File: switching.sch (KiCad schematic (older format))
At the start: 0 parts

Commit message: Added switching, still need arduino verification, need buffer, consisder PSU polarity switch
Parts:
- added D? (x4): 1N914, symbol Device:D
- added J?: Screw_Terminal_01x05, symbol Connector:Screw_Terminal_01x05
- added K? (x4): RM50-xx21, Relay_THT:Relay_SPST_Finder_32.21-x300, symbol Relay:RM50-xx21
- added Q? (x4): 2N3904, Package_TO_SOT_THT:TO-92_Inline, symbol Transistor_BJT:2N3904
- added R? (x4): 1k, symbol Device:R
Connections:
- new net: J?.1 (Pin_1), K?.11
- new net: J?.5 (Pin_5), K?.14, K?.14, K?.14, K?.14
- new net: D?.2 (A), K?.A1, Q?.3 (C) (x4)
- new net: J?.2 (Pin_2), K?.11
- new net: J?.3 (Pin_3), K?.11
- new net: J?.4 (Pin_4), K?.11
- new net: Q?.2 (B), R?.1 (x4)
- new net +9V: D?.1 (K), D?.1 (K), D?.1 (K), D?.1 (K), K?.A2, K?.A2, K?.A2, K?.A2
- new net GND: Q?.1 (E), Q?.1 (E), Q?.1 (E), Q?.1 (E)
- new net RLY0: R?.2
- new net RLY1: R?.2
- new net RLY2: R?.2
- new net RLY3: R?.2

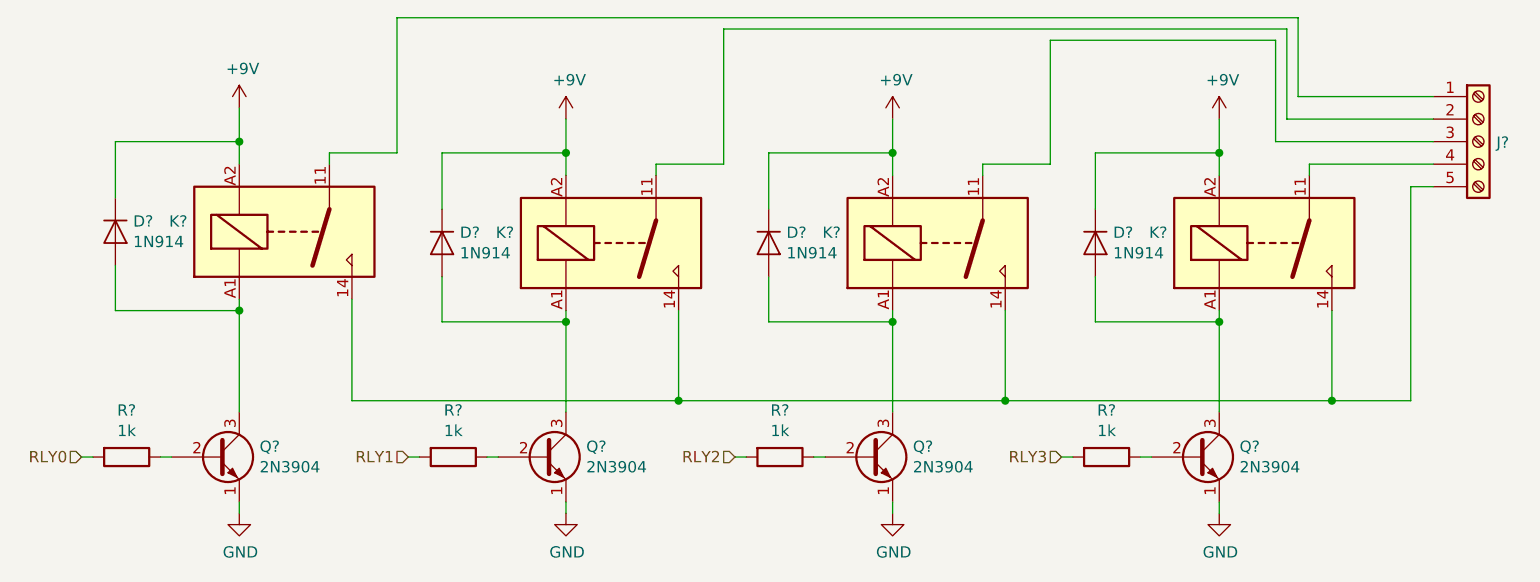
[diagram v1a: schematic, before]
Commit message: Schem entry done, need to do footprints and PCB
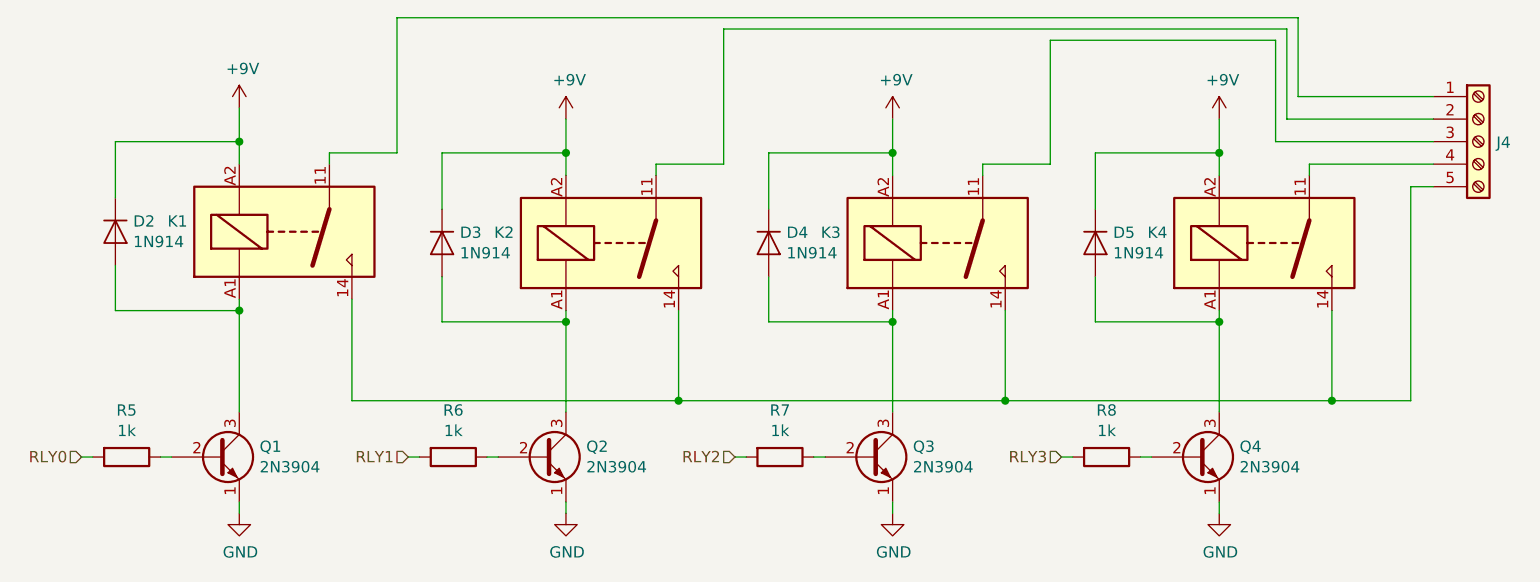
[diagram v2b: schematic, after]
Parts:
- gave numbers to parts that had none: 17
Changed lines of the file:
@@
 EESchema Schematic File Version 4
 LIBS:midi_switcher-cache
-EELAYER 29 0
+EELAYER 30 0
 EELAYER END
 $Descr A4 11693 8268
@@
 $EndDescr
 $Comp
-L Relay:RM50-xx21 K?
+L Relay:RM50-xx21 K1
 U 1 1 5DC03F87
 P 3650 3000
-F 0 "K?" H 3220 2954 50  0000 R CNN
+F 0 "K1" H 3220 2954 50  0000 R CNN
 F 1 "RM50-xx21" H 3900 3300 50  0001 R CNN
 F 2 "Relay_THT:Relay_SPST_Finder_32.21-x300" H 4920 2970 50  0001 C CNN
@@
 $EndComp
 $Comp
-L Device:D D?
+L Device:D D2
 U 1 1 5DC05805
 P 2900 3000
-F 0 "D?" V 2854 3079 50  0000 L CNN
+F 0 "D2" V 2854 3079 50  0000 L CNN
 F 1 "1N914" V 2945 3079 50  0000 L CNN
 F 2 "" H 2900 3000 50  0001 C CNN
@@
 Connection ~ 3450 2600
 $Comp
-L Relay:RM50-xx21 K?
+L Relay:RM50-xx21 K2
 U 1 1 5DC08AA8
 P 5100 3050
-F 0 "K?" H 4670 3004 50  0000 R CNN
+F 0 "K2" H 4670 3004 50  0000 R CNN
 F 1 "RM50-xx21" H 5350 3350 50  0001 R CNN
 F 2 "Relay_THT:Relay_SPST_Finder_32.21-x300" H 6370 3020 50  0001 C CNN
@@
 $EndComp
 $Comp
-L Device:D D?
+L Device:D D3
 U 1 1 5DC08ABC
 P 4350 3050
-F 0 "D?" V 4304 3129 50  0000 L CNN
+F 0 "D3" V 4304 3129 50  0000 L CNN
 F 1 "1N914" V 4395 3129 50  0000 L CNN
 F 2 "" H 4350 3050 50  0001 C CNN
@@
 Connection ~ 4900 2650
 $Comp
-L Relay:RM50-xx21 K?
+L Relay:RM50-xx21 K3
 U 1 1 5DC0D594
 P 6550 3050
-F 0 "K?" H 6120 3004 50  0000 R CNN
+F 0 "K3" H 6120 3004 50  0000 R CNN
 F 1 "RM50-xx21" H 6800 3350 50  0001 R CNN
 F 2 "Relay_THT:Relay_SPST_Finder_32.21-x300" H 7820 3020 50  0001 C CNN
@@
 $EndComp
 $Comp
-L Device:D D?
+L Device:D D4
 U 1 1 5DC0D5A0
 P 5800 3050
-F 0 "D?" V 5754 3129 50  0000 L CNN
+F 0 "D4" V 5754 3129 50  0000 L CNN
 F 1 "1N914" V 5845 3129 50  0000 L CNN
 F 2 "" H 5800 3050 50  0001 C CNN
@@
 Connection ~ 6350 2650
 $Comp
-L Relay:RM50-xx21 K?
+L Relay:RM50-xx21 K4
 U 1 1 5DC0EA27
 P 8000 3050
-F 0 "K?" H 7570 3004 50  0000 R CNN
+F 0 "K4" H 7570 3004 50  0000 R CNN
 F 1 "RM50-xx21" H 8250 3350 50  0001 R CNN
 F 2 "Relay_THT:Relay_SPST_Finder_32.21-x300" H 9270 3020 50  0001 C CNN
@@
 $EndComp
 $Comp
-L Device:D D?
+L Device:D D5
 U 1 1 5DC0EA33
 P 7250 3050
-F 0 "D?" V 7204 3129 50  0000 L CNN
+F 0 "D5" V 7204 3129 50  0000 L CNN
 F 1 "1N914" V 7295 3129 50  0000 L CNN
 F 2 "" H 7250 3050 50  0001 C CNN
@@
 Connection ~ 6850 3750
 $Comp
-L Connector:Screw_Terminal_01x05 J?
+L Connector:Screw_Terminal_01x05 J4
 U 1 1 5DC1162A
 P 8950 2600
-F 0 "J?" H 9030 2596 50  0000 L CNN
+F 0 "J4" H 9030 2596 50  0000 L CNN
 F 1 "Screw_Terminal_01x05" H 9030 2551 50  0001 L CNN
 F 2 "" H 8950 2600 50  0001 C CNN
@@
 	4150 2050 4150 2650
 $Comp
-L power:+9V #PWR?
+L power:+9V #PWR0116
 U 1 1 5DC19F00
 P 3450 2450
-F 0 "#PWR?" H 3450 2300 50  0001 C CNN
+F 0 "#PWR0116" H 3450 2300 50  0001 C CNN
 F 1 "+9V" H 3465 2623 50  0000 C CNN
 F 2 "" H 3450 2450 50  0001 C CNN
@@
 $EndComp
 $Comp
-L power:+9V #PWR?
+L power:+9V #PWR0117
 U 1 1 5DC1A6B9
 P 4900 2500
-F 0 "#PWR?" H 4900 2350 50  0001 C CNN
+F 0 "#PWR0117" H 4900 2350 50  0001 C CNN
 F 1 "+9V" H 4915 2673 50  0000 C CNN
 F 2 "" H 4900 2500 50  0001 C CNN
@@
 $EndComp
 $Comp
-L power:+9V #PWR?
+L power:+9V #PWR0118
 U 1 1 5DC1AC7E
 P 6350 2500
-F 0 "#PWR?" H 6350 2350 50  0001 C CNN
+F 0 "#PWR0118" H 6350 2350 50  0001 C CNN
 F 1 "+9V" H 6365 2673 50  0000 C CNN
 F 2 "" H 6350 2500 50  0001 C CNN
@@
 $EndComp
 $Comp
-L power:+9V #PWR?
+L power:+9V #PWR0119
 U 1 1 5DC1B0BC
 P 7800 2500
-F 0 "#PWR?" H 7800 2350 50  0001 C CNN
+F 0 "#PWR0119" H 7800 2350 50  0001 C CNN
 F 1 "+9V" H 7815 2673 50  0000 C CNN
 F 2 "" H 7800 2500 50  0001 C CNN
@@
 $EndComp
 $Comp
-L Transistor_BJT:2N3904 Q?
+L Transistor_BJT:2N3904 Q1
 U 1 1 5DC1BD59
 P 3350 4000
-F 0 "Q?" H 3540 4046 50  0000 L CNN
+F 0 "Q1" H 3540 4046 50  0000 L CNN
 F 1 "2N3904" H 3540 3955 50  0000 L CNN
 F 2 "Package_TO_SOT_THT:TO-92_Inline" H 3550 3925 50  0001 L CIN
@@
 $EndComp
 $Comp
-L Transistor_BJT:2N3904 Q?
+L Transistor_BJT:2N3904 Q2
 U 1 1 5DC1CB65
 P 4800 4000
-F 0 "Q?" H 4990 4046 50  0000 L CNN
+F 0 "Q2" H 4990 4046 50  0000 L CNN
 F 1 "2N3904" H 4990 3955 50  0000 L CNN
 F 2 "Package_TO_SOT_THT:TO-92_Inline" H 5000 3925 50  0001 L CIN
@@
 $EndComp
 $Comp
-L Transistor_BJT:2N3904 Q?
+L Transistor_BJT:2N3904 Q3
 U 1 1 5DC1D7A9
 P 6250 4000
-F 0 "Q?" H 6440 4046 50  0000 L CNN
+F 0 "Q3" H 6440 4046 50  0000 L CNN
 F 1 "2N3904" H 6440 3955 50  0000 L CNN
 F 2 "Package_TO_SOT_THT:TO-92_Inline" H 6450 3925 50  0001 L CIN
@@
 $EndComp
 $Comp
-L Transistor_BJT:2N3904 Q?
+L Transistor_BJT:2N3904 Q4
 U 1 1 5DC1E450
 P 7700 4000
-F 0 "Q?" H 7890 4046 50  0000 L CNN
+F 0 "Q4" H 7890 4046 50  0000 L CNN
 F 1 "2N3904" H 7890 3955 50  0000 L CNN
 F 2 "Package_TO_SOT_THT:TO-92_Inline" H 7900 3925 50  0001 L CIN
@@
 $EndComp
 $Comp
-L Device:R R?
+L Device:R R5
 U 1 1 5DC24854
 P 2950 4000
-F 0 "R?" V 2743 4000 50  0000 C CNN
+F 0 "R5" V 2743 4000 50  0000 C CNN
 F 1 "1k" V 2834 4000 50  0000 C CNN
 F 2 "" V 2880 4000 50  0001 C CNN
@@
 $EndComp
 $Comp
-L Device:R R?
+L Device:R R6
 U 1 1 5DC25203
 P 4400 4000
-F 0 "R?" V 4193 4000 50  0000 C CNN
+F 0 "R6" V 4193 4000 50  0000 C CNN
 F 1 "1k" V 4284 4000 50  0000 C CNN
 F 2 "" V 4330 4000 50  0001 C CNN
@@
 $EndComp
 $Comp
-L Device:R R?
+L Device:R R7
 U 1 1 5DC25738
 P 5850 4000
-F 0 "R?" V 5643 4000 50  0000 C CNN
+F 0 "R7" V 5643 4000 50  0000 C CNN
 F 1 "1k" V 5734 4000 50  0000 C CNN
 F 2 "" V 5780 4000 50  0001 C CNN
@@
 $EndComp
 $Comp
-L Device:R R?
+L Device:R R8
 U 1 1 5DC25D8A
 P 7300 4000
-F 0 "R?" V 7093 4000 50  0000 C CNN
+F 0 "R8" V 7093 4000 50  0000 C CNN
 F 1 "1k" V 7184 4000 50  0000 C CNN
 F 2 "" V 7230 4000 50  0001 C CNN
@@
 	3450 3350 3450 3800
 $Comp
-L power:GND #PWR?
+L power:GND #PWR0120
 U 1 1 5DC34E53
 P 3450 4250
-F 0 "#PWR?" H 3450 4000 50  0001 C CNN
+F 0 "#PWR0120" H 3450 4000 50  0001 C CNN
 F 1 "GND" H 3455 4077 50  0000 C CNN
 F 2 "" H 3450 4250 50  0001 C CNN
@@
 	3450 4200 3450 4250
 $Comp
-L power:GND #PWR?
+L power:GND #PWR0121
 U 1 1 5DC36B1E
 P 4900 4250
-F 0 "#PWR?" H 4900 4000 50  0001 C CNN
+F 0 "#PWR0121" H 4900 4000 50  0001 C CNN
 F 1 "GND" H 4905 4077 50  0000 C CNN
 F 2 "" H 4900 4250 50  0001 C CNN
@@
 $EndComp
 $Comp
-L power:GND #PWR?
+L power:GND #PWR0122
 U 1 1 5DC370B8
 P 6350 4250
-F 0 "#PWR?" H 6350 4000 50  0001 C CNN
+F 0 "#PWR0122" H 6350 4000 50  0001 C CNN
 F 1 "GND" H 6355 4077 50  0000 C CNN
 F 2 "" H 6350 4250 50  0001 C CNN
@@
 $EndComp
 $Comp
-L power:GND #PWR?
+L power:GND #PWR0123
 U 1 1 5DC3769E
 P 7800 4250
-F 0 "#PWR?" H 7800 4000 50  0001 C CNN
+F 0 "#PWR0123" H 7800 4000 50  0001 C CNN
 F 1 "GND" H 7805 4077 50  0000 C CNN
 F 2 "" H 7800 4250 50  0001 C CNN

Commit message: pushing for work to do over holiday
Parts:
- removed K2, K3, K4: RM50-xx21, Relay_THT:Relay_SPST_Finder_32.21-x300, symbol Relay:RM50-xx21
- removed Q1, Q2, Q3, Q4: 2N3904, Package_TO_SOT_THT:TO-92_Inline, symbol Transistor_BJT:2N3904
- added K2, K3, K4: RM50-xx21, Relay_THT:Relay_SPST_Omron-G5Q-1A, symbol Relay:TE_PCH-1xxx2M
- added Q1, Q2, Q3, Q4: BC337, Package_TO_SOT_THT:TO-92_Inline, symbol Transistor_BJT:BC337
- D2, D3, D4, D5: footprint (none) -> Diode_THT:D_DO-35_SOD27_P10.16mm_Horizontal
- J4: footprint (none) -> TerminalBlock:TerminalBlock_bornier-5_P5.08mm
- K1: footprint Relay_THT:Relay_SPST_Finder_32.21-x300 -> Relay_THT:Relay_SPST_Omron-G5Q-1A; symbol Relay:RM50-xx21 -> Relay:TE_PCH-1xxx2M
- R5, R6, R7, R8: footprint (none) -> Resistor_THT:R_Axial_DIN0207_L6.3mm_D2.5mm_P10.16mm_Horizontal
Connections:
- net +9V: now also K1.1, K2.1, K3.1, K4.1; no longer K1.A2
- net GND: now also Q1.3 (E), Q2.3 (E), Q3.3 (E), Q4.3 (E)
- net RLY0: now also R8.2; no longer R5.2
- net RLY1: now also R7.2; no longer R6.2
- net RLY2: now also R6.2; no longer R7.2
- net RLY3: now also R5.2; no longer R8.2
- net at J4.1 (Pin_1): now also K1.2; no longer K1.11
- net at J4.5 (Pin_5): now also K1.3, K2.3, K3.3, K4.3; no longer K1.14
- net at D2.2 (A): now also K1.5, Q1.1 (C); no longer K1.A1
- net at J4.2 (Pin_2): now also K2.2
- net at D3.2 (A): now also K2.5, Q2.1 (C)
- net at J4.3 (Pin_3): now also K3.2
- net at D4.2 (A): now also K3.5, Q3.1 (C)
- net at J4.4 (Pin_4): now also K4.2
- net at D5.2 (A): now also K4.5, Q4.1 (C)
- net at R5.1: now also Q1.2 (B)
- net at R6.1: now also Q2.2 (B)
- net at R7.1: now also Q3.2 (B)
- net at R8.1: now also Q4.2 (B)
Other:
- moved on the sheet: K1
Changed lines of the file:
@@
 EESchema Schematic File Version 4
 LIBS:midi_switcher-cache
-EELAYER 30 0
+EELAYER 29 0
 EELAYER END
 $Descr A4 11693 8268
@@
 $EndDescr
 $Comp
-L Relay:RM50-xx21 K1
+L Relay:TE_PCH-1xxx2M K1
 U 1 1 5DC03F87
 P 3650 3000
 F 0 "K1" H 3220 2954 50  0000 R CNN
 F 1 "RM50-xx21" H 3900 3300 50  0001 R CNN
-F 2 "Relay_THT:Relay_SPST_Finder_32.21-x300" H 4920 2970 50  0001 C CNN
+F 2 "Relay_THT:Relay_SPST_Omron-G5Q-1A" H 4920 2970 50  0001 C CNN
 F 3 "http://www.relpol.pl/en/content/download/13683/165953/file/e_RM50.pdf" H 3650 3000 50  0001 C CNN
 	1    3650 3000
@@
 F 0 "D2" V 2854 3079 50  0000 L CNN
 F 1 "1N914" V 2945 3079 50  0000 L CNN
-F 2 "" H 2900 3000 50  0001 C CNN
+F 2 "Diode_THT:D_DO-35_SOD27_P10.16mm_Horizontal" H 2900 3000 50  0001 C CNN
 F 3 "~" H 2900 3000 50  0001 C CNN
 	1    2900 3000
@@
 Wire Wire Line
 	3850 2650 3850 2700
-Text HLabel 2750 4000 0    50   Input ~ 0
+Text HLabel 7100 4000 0    50   Input ~ 0
 RLY0
 Wire Wire Line
 	3450 2600 3450 2450
 Connection ~ 3450 2600
-$Comp
-L Relay:RM50-xx21 K2
-U 1 1 5DC08AA8
-P 5100 3050
-F 0 "K2" H 4670 3004 50  0000 R CNN
-F 1 "RM50-xx21" H 5350 3350 50  0001 R CNN
-F 2 "Relay_THT:Relay_SPST_Finder_32.21-x300" H 6370 3020 50  0001 C CNN
-F 3 "http://www.relpol.pl/en/content/download/13683/165953/file/e_RM50.pdf" H 5100 3050 50  0001 C CNN
-	1    5100 3050
-	1    0    0    1
-$EndComp
 $Comp
 L Device:D D3
@@
 F 0 "D3" V 4304 3129 50  0000 L CNN
 F 1 "1N914" V 4395 3129 50  0000 L CNN
-F 2 "" H 4350 3050 50  0001 C CNN
+F 2 "Diode_THT:D_DO-35_SOD27_P10.16mm_Horizontal" H 4350 3050 50  0001 C CNN
 F 3 "~" H 4350 3050 50  0001 C CNN
 	1    4350 3050
@@
 Wire Wire Line
 	5300 2700 5300 2750
-Text HLabel 4200 4000 0    50   Input ~ 0
+Text HLabel 5650 4000 0    50   Input ~ 0
 RLY1
 Wire Wire Line
 	4900 2650 4900 2500
 Connection ~ 4900 2650
-$Comp
-L Relay:RM50-xx21 K3
-U 1 1 5DC0D594
-P 6550 3050
-F 0 "K3" H 6120 3004 50  0000 R CNN
-F 1 "RM50-xx21" H 6800 3350 50  0001 R CNN
-F 2 "Relay_THT:Relay_SPST_Finder_32.21-x300" H 7820 3020 50  0001 C CNN
-F 3 "http://www.relpol.pl/en/content/download/13683/165953/file/e_RM50.pdf" H 6550 3050 50  0001 C CNN
-	1    6550 3050
-	1    0    0    1
-$EndComp
 $Comp
 L Device:D D4
@@
 F 0 "D4" V 5754 3129 50  0000 L CNN
 F 1 "1N914" V 5845 3129 50  0000 L CNN
-F 2 "" H 5800 3050 50  0001 C CNN
+F 2 "Diode_THT:D_DO-35_SOD27_P10.16mm_Horizontal" H 5800 3050 50  0001 C CNN
 F 3 "~" H 5800 3050 50  0001 C CNN
 	1    5800 3050
@@
 Wire Wire Line
 	6750 2700 6750 2750
-Text HLabel 5650 4000 0    50   Input ~ 0
+Text HLabel 4200 4000 0    50   Input ~ 0
 RLY2
 Wire Wire Line
 	6350 2650 6350 2500
 Connection ~ 6350 2650
-$Comp
-L Relay:RM50-xx21 K4
-U 1 1 5DC0EA27
-P 8000 3050
-F 0 "K4" H 7570 3004 50  0000 R CNN
-F 1 "RM50-xx21" H 8250 3350 50  0001 R CNN
-F 2 "Relay_THT:Relay_SPST_Finder_32.21-x300" H 9270 3020 50  0001 C CNN
-F 3 "http://www.relpol.pl/en/content/download/13683/165953/file/e_RM50.pdf" H 8000 3050 50  0001 C CNN
-	1    8000 3050
-	1    0    0    1
-$EndComp
 $Comp
 L Device:D D5
@@
 F 0 "D5" V 7204 3129 50  0000 L CNN
 F 1 "1N914" V 7295 3129 50  0000 L CNN
-F 2 "" H 7250 3050 50  0001 C CNN
+F 2 "Diode_THT:D_DO-35_SOD27_P10.16mm_Horizontal" H 7250 3050 50  0001 C CNN
 F 3 "~" H 7250 3050 50  0001 C CNN
 	1    7250 3050
@@
 Wire Wire Line
 	8200 2700 8200 2750
-Text HLabel 7100 4000 0    50   Input ~ 0
+Text HLabel 2750 4000 0    50   Input ~ 0
 RLY3
 Wire Wire Line
@@
 Connection ~ 7800 2650
 Wire Wire Line
-	3950 3750 5400 3750
-Wire Wire Line
-	3950 3300 3950 3750
-Wire Wire Line
-	5400 3350 5400 3750
-Wire Wire Line
-	5400 3750 6850 3750
-Wire Wire Line
-	6850 3350 6850 3750
-Connection ~ 5400 3750
-Wire Wire Line
-	6850 3750 8300 3750
-Wire Wire Line
-	8300 3350 8300 3750
-Connection ~ 6850 3750
+	3850 3300 3850 3750
 $Comp
 L Connector:Screw_Terminal_01x05 J4
@@
 F 0 "J4" H 9030 2596 50  0000 L CNN
 F 1 "Screw_Terminal_01x05" H 9030 2551 50  0001 L CNN
-F 2 "" H 8950 2600 50  0001 C CNN
+F 2 "TerminalBlock:TerminalBlock_bornier-5_P5.08mm" H 8950 2600 50  0001 C CNN
 F 3 "~" H 8950 2600 50  0001 C CNN
 	1    8950 2600
@@
 $EndComp
 Wire Wire Line
-	8300 3750 8650 3750
-Wire Wire Line
 	8650 3750 8650 2800
 Wire Wire Line
 	8650 2800 8750 2800
-Connection ~ 8300 3750
 Wire Wire Line
 	8200 2700 8750 2700
@@
 $EndComp
 $Comp
-L Transistor_BJT:2N3904 Q1
-U 1 1 5DC1BD59
-P 3350 4000
-F 0 "Q1" H 3540 4046 50  0000 L CNN
-F 1 "2N3904" H 3540 3955 50  0000 L CNN
-F 2 "Package_TO_SOT_THT:TO-92_Inline" H 3550 3925 50  0001 L CIN
-F 3 "https://www.fairchildsemi.com/datasheets/2N/2N3904.pdf" H 3350 4000 50  0001 L CNN
-	1    3350 4000
-	1    0    0    -1
-$EndComp
-$Comp
-L Transistor_BJT:2N3904 Q2
-U 1 1 5DC1CB65
-P 4800 4000
-F 0 "Q2" H 4990 4046 50  0000 L CNN
-F 1 "2N3904" H 4990 3955 50  0000 L CNN
-F 2 "Package_TO_SOT_THT:TO-92_Inline" H 5000 3925 50  0001 L CIN
-F 3 "https://www.fairchildsemi.com/datasheets/2N/2N3904.pdf" H 4800 4000 50  0001 L CNN
-	1    4800 4000
-	1    0    0    -1
-$EndComp
-$Comp
-L Transistor_BJT:2N3904 Q3
-U 1 1 5DC1D7A9
-P 6250 4000
-F 0 "Q3" H 6440 4046 50  0000 L CNN
-F 1 "2N3904" H 6440 3955 50  0000 L CNN
-F 2 "Package_TO_SOT_THT:TO-92_Inline" H 6450 3925 50  0001 L CIN
-F 3 "https://www.fairchildsemi.com/datasheets/2N/2N3904.pdf" H 6250 4000 50  0001 L CNN
-	1    6250 4000
-	1    0    0    -1
-$EndComp
-$Comp
-L Transistor_BJT:2N3904 Q4
-U 1 1 5DC1E450
-P 7700 4000
-F 0 "Q4" H 7890 4046 50  0000 L CNN
-F 1 "2N3904" H 7890 3955 50  0000 L CNN
-F 2 "Package_TO_SOT_THT:TO-92_Inline" H 7900 3925 50  0001 L CIN
-F 3 "https://www.fairchildsemi.com/datasheets/2N/2N3904.pdf" H 7700 4000 50  0001 L CNN
-	1    7700 4000
-	1    0    0    -1
-$EndComp
-$Comp
 L Device:R R5
 U 1 1 5DC24854
@@
 F 0 "R5" V 2743 4000 50  0000 C CNN
 F 1 "1k" V 2834 4000 50  0000 C CNN
-F 2 "" V 2880 4000 50  0001 C CNN
+F 2 "Resistor_THT:R_Axial_DIN0207_L6.3mm_D2.5mm_P10.16mm_Horizontal" V 2880 4000 50  0001 C CNN
 F 3 "~" H 2950 4000 50  0001 C CNN
 	1    2950 4000
@@
 F 0 "R6" V 4193 4000 50  0000 C CNN
 F 1 "1k" V 4284 4000 50  0000 C CNN
-F 2 "" V 4330 4000 50  0001 C CNN
+F 2 "Resistor_THT:R_Axial_DIN0207_L6.3mm_D2.5mm_P10.16mm_Horizontal" V 4330 4000 50  0001 C CNN
 F 3 "~" H 4400 4000 50  0001 C CNN
 	1    4400 4000
@@
 F 0 "R7" V 5643 4000 50  0000 C CNN
 F 1 "1k" V 5734 4000 50  0000 C CNN
-F 2 "" V 5780 4000 50  0001 C CNN
+F 2 "Resistor_THT:R_Axial_DIN0207_L6.3mm_D2.5mm_P10.16mm_Horizontal" V 5780 4000 50  0001 C CNN
 F 3 "~" H 5850 4000 50  0001 C CNN
 	1    5850 4000
@@
 F 0 "R8" V 7093 4000 50  0000 C CNN
 F 1 "1k" V 7184 4000 50  0000 C CNN
-F 2 "" V 7230 4000 50  0001 C CNN
+F 2 "Resistor_THT:R_Axial_DIN0207_L6.3mm_D2.5mm_P10.16mm_Horizontal" V 7230 4000 50  0001 C CNN
 F 3 "~" H 7300 4000 50  0001 C CNN
 	1    7300 4000
@@
 Wire Wire Line
 	4900 4250 4900 4200
+$Comp
+L Transistor_BJT:BC337 Q1
+U 1 1 5DCB61AF
+P 3350 4000
+F 0 "Q1" H 3541 4046 50  0000 L CNN
+F 1 "BC337" H 3541 3955 50  0000 L CNN
+F 2 "Package_TO_SOT_THT:TO-92_Inline" H 3550 3925 50  0001 L CIN
+F 3 "https://diotec.com/tl_files/diotec/files/pdf/datasheets/bc337.pdf" H 3350 4000 50  0001 L CNN
+	1    3350 4000
+	1    0    0    -1
+$EndComp
+$Comp
+L Transistor_BJT:BC337 Q2
+U 1 1 5DCB891E
+P 4800 4000
+F 0 "Q2" H 4991 4046 50  0000 L CNN
+F 1 "BC337" H 4991 3955 50  0000 L CNN
+F 2 "Package_TO_SOT_THT:TO-92_Inline" H 5000 3925 50  0001 L CIN
+F 3 "https://diotec.com/tl_files/diotec/files/pdf/datasheets/bc337.pdf" H 4800 4000 50  0001 L CNN
+	1    4800 4000
+	1    0    0    -1
+$EndComp
+$Comp
+L Transistor_BJT:BC337 Q3
+U 1 1 5DCB96F8
+P 6250 4000
+F 0 "Q3" H 6441 4046 50  0000 L CNN
+F 1 "BC337" H 6441 3955 50  0000 L CNN
+F 2 "Package_TO_SOT_THT:TO-92_Inline" H 6450 3925 50  0001 L CIN
+F 3 "https://diotec.com/tl_files/diotec/files/pdf/datasheets/bc337.pdf" H 6250 4000 50  0001 L CNN
+	1    6250 4000
+	1    0    0    -1
+$EndComp
+$Comp
+L Transistor_BJT:BC337 Q4
+U 1 1 5DCBA831
+P 7700 4000
+F 0 "Q4" H 7891 4046 50  0000 L CNN
+F 1 "BC337" H 7891 3955 50  0000 L CNN
+F 2 "Package_TO_SOT_THT:TO-92_Inline" H 7900 3925 50  0001 L CIN
+F 3 "https://diotec.com/tl_files/diotec/files/pdf/datasheets/bc337.pdf" H 7700 4000 50  0001 L CNN
+	1    7700 4000
+	1    0    0    -1
+$EndComp
+$Comp
+L Relay:TE_PCH-1xxx2M K2
+U 1 1 5DCCE202
+P 5100 3050
+F 0 "K2" H 4670 3004 50  0000 R CNN
+F 1 "RM50-xx21" H 5350 3350 50  0001 R CNN
+F 2 "Relay_THT:Relay_SPST_Omron-G5Q-1A" H 6370 3020 50  0001 C CNN
+F 3 "http://www.relpol.pl/en/content/download/13683/165953/file/e_RM50.pdf" H 5100 3050 50  0001 C CNN
+	1    5100 3050
+	1    0    0    1
+$EndComp
+$Comp
+L Relay:TE_PCH-1xxx2M K3
+U 1 1 5DCCF58D
+P 6550 3050
+F 0 "K3" H 6120 3004 50  0000 R CNN
+F 1 "RM50-xx21" H 6800 3350 50  0001 R CNN
+F 2 "Relay_THT:Relay_SPST_Omron-G5Q-1A" H 7820 3020 50  0001 C CNN
+F 3 "http://www.relpol.pl/en/content/download/13683/165953/file/e_RM50.pdf" H 6550 3050 50  0001 C CNN
+	1    6550 3050
+	1    0    0    1
+$EndComp
+$Comp
+L Relay:TE_PCH-1xxx2M K4
+U 1 1 5DCD07E7
+P 8000 3050
+F 0 "K4" H 7570 3004 50  0000 R CNN
+F 1 "RM50-xx21" H 8250 3350 50  0001 R CNN
+F 2 "Relay_THT:Relay_SPST_Omron-G5Q-1A" H 9270 3020 50  0001 C CNN
+F 3 "http://www.relpol.pl/en/content/download/13683/165953/file/e_RM50.pdf" H 8000 3050 50  0001 C CNN
+	1    8000 3050
+	1    0    0    1
+$EndComp
+Wire Wire Line
+	3850 3750 5300 3750
+Wire Wire Line
+	5300 3350 5300 3750
+Connection ~ 5300 3750
+Wire Wire Line
+	5300 3750 6750 3750
+Wire Wire Line
+	6750 3350 6750 3750
+Connection ~ 6750 3750
+Wire Wire Line
+	6750 3750 8200 3750
+Wire Wire Line
+	8200 3350 8200 3750
+Connection ~ 8200 3750
+Wire Wire Line
+	8200 3750 8650 3750
 $EndSCHEMATC
